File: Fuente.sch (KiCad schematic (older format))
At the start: 14 parts, among them IC1 LM2577HV-ADJ, J1 CONN_01X02, U3 LM7805

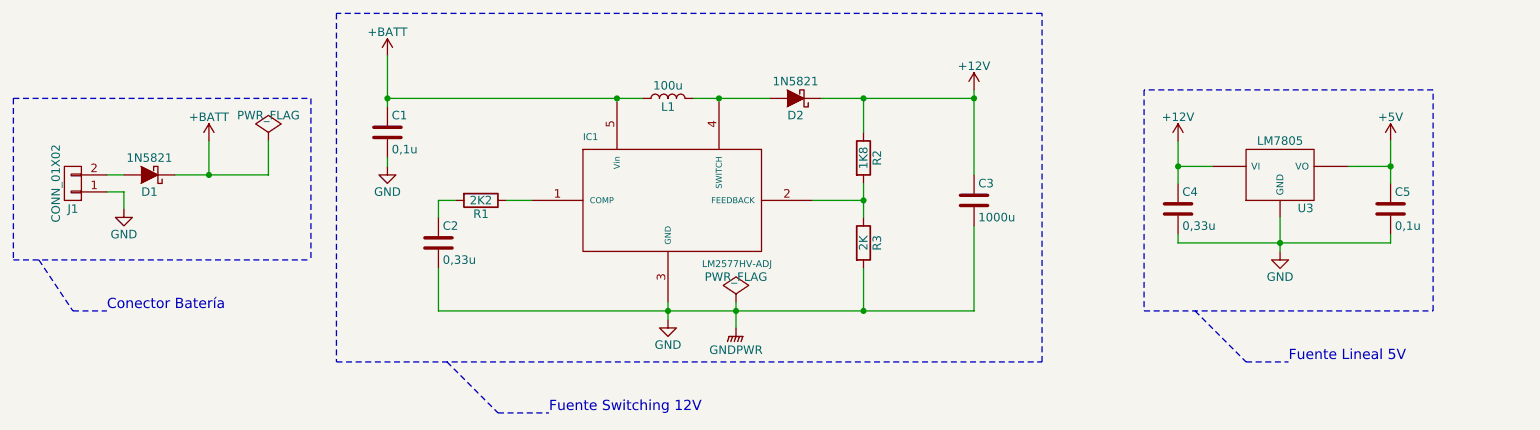
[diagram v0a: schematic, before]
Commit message: Reestructuracion de hojas de esquematico.
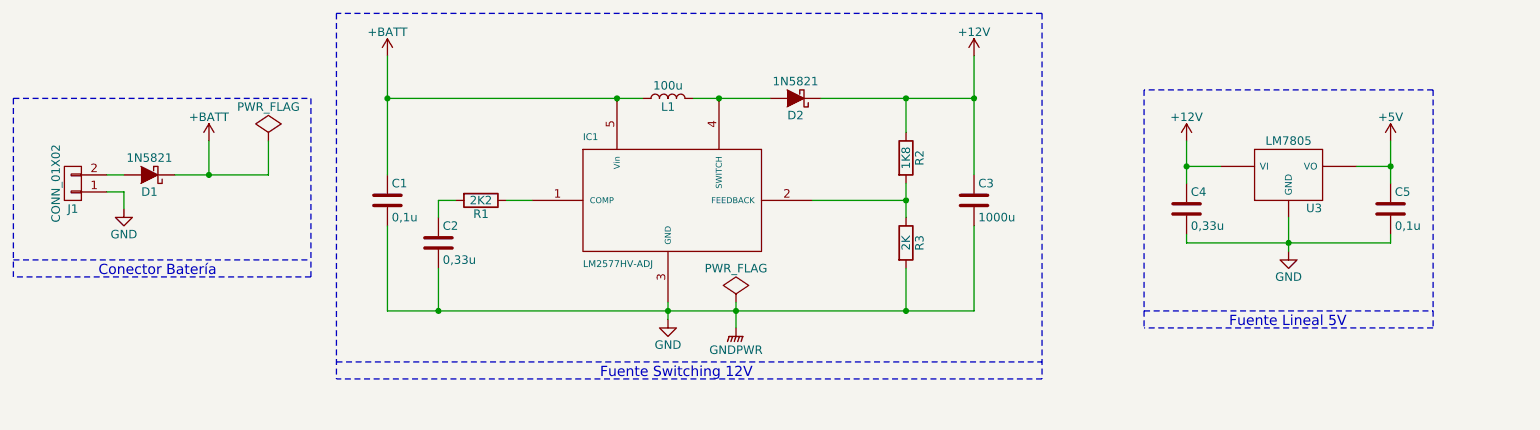
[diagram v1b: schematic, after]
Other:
- moved on the sheet: C1, C4, R2, R3, U3
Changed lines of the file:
@@
 LIBS:contrib
 LIBS:valves
-LIBS:Poncho_Esqueleto
 LIBS:LM2577HV-ADJ
 LIBS:pololu_a4988
@@
 $Descr A4 11693 8268
 encoding utf-8
-Sheet 3 4
+Sheet 3 2
 Title ""
 Date "2017-05-09"
@@
 P 5700 3600
 F 0 "IC1" H 5200 3900 40  0000 L BNN
-F 1 "LM2577HV-ADJ" H 5900 3200 40  0000 L TNN
+F 1 "LM2577HV-ADJ" H 5200 3200 40  0000 L TNN
 F 2 "" H 7300 3450 30  0000 C CIN
 F 3 "" H 7300 3450 60  0000 C CNN
@@
 L R R3
 U 1 1 59114DCA
-P 6850 3900
-F 0 "R3" V 6930 3900 50  0000 C CNN
-F 1 "2K" V 6850 3900 50  0000 C CNN
-F 2 "" V 6780 3900 50  0001 C CNN
-F 3 "" H 6850 3900 50  0001 C CNN
-	1    6850 3900
+P 7100 3900
+F 0 "R3" V 7180 3900 50  0000 C CNN
+F 1 "2K" V 7100 3900 50  0000 C CNN
+F 2 "" V 7030 3900 50  0001 C CNN
+F 3 "" H 7100 3900 50  0001 C CNN
+	1    7100 3900
 	1    0    0    -1
 $EndComp
@@
 L R R2
 U 1 1 59114DE9
-P 6850 3400
-F 0 "R2" V 6930 3400 50  0000 C CNN
-F 1 "1K8" V 6850 3400 50  0000 C CNN
-F 2 "" V 6780 3400 50  0001 C CNN
-F 3 "" H 6850 3400 50  0001 C CNN
-	1    6850 3400
+P 7100 3400
+F 0 "R2" V 7180 3400 50  0000 C CNN
+F 1 "1K8" V 7100 3400 50  0000 C CNN
+F 2 "" V 7030 3400 50  0001 C CNN
+F 3 "" H 7100 3400 50  0001 C CNN
+	1    7100 3400
 	1    0    0    -1
 $EndComp
@@
 L +12V #PWR010
 U 1 1 5911531B
-P 7500 3000
-F 0 "#PWR010" H 7500 2850 50  0001 C CNN
-F 1 "+12V" H 7500 3140 50  0000 C CNN
-F 2 "" H 7500 3000 50  0001 C CNN
-F 3 "" H 7500 3000 50  0001 C CNN
-	1    7500 3000
+P 7500 2800
+F 0 "#PWR010" H 7500 2650 50  0001 C CNN
+F 1 "+12V" H 7500 2940 50  0000 C CNN
+F 2 "" H 7500 2800 50  0001 C CNN
+F 3 "" H 7500 2800 50  0001 C CNN
+	1    7500 2800
 	1    0    0    -1
 $EndComp
@@
 L C C1
 U 1 1 59115966
-P 4050 3250
-F 0 "C1" H 4075 3350 50  0000 L CNN
-F 1 "0,1u" H 4075 3150 50  0000 L CNN
-F 2 "" H 4088 3100 50  0001 C CNN
-F 3 "" H 4050 3250 50  0001 C CNN
-	1    4050 3250
-	1    0    0    -1
-$EndComp
-$Comp
-L GND #PWR011
-U 1 1 591159FB
-P 4050 3450
-F 0 "#PWR011" H 4050 3200 50  0001 C CNN
-F 1 "GND" H 4050 3300 50  0000 C CNN
-F 2 "" H 4050 3450 50  0001 C CNN
-F 3 "" H 4050 3450 50  0001 C CNN
-	1    4050 3450
+P 4050 3650
+F 0 "C1" H 4075 3750 50  0000 L CNN
+F 1 "0,1u" H 4075 3550 50  0000 L CNN
+F 2 "" H 4088 3500 50  0001 C CNN
+F 3 "" H 4050 3650 50  0001 C CNN
+	1    4050 3650
 	1    0    0    -1
 $EndComp
@@
 	5700 4350 5700 4250
 Wire Wire Line
-	6850 3550 6850 3750
-Wire Wire Line
-	6550 3650 6850 3650
-Connection ~ 6850 3650
-Wire Wire Line
-	6850 4050 6850 4300
-Wire Wire Line
-	4350 4300 7500 4300
+	4050 4300 7500 4300
 Connection ~ 5700 4300
 Wire Wire Line
@@
 Wire Wire Line
 	6600 3050 7500 3050
-Wire Wire Line
-	6850 3050 6850 3250
 Connection ~ 6000 3050
 Wire Wire Line
-	7500 3000 7500 3500
-Connection ~ 6850 3050
-Connection ~ 6850 4300
+	7500 2800 7500 3500
 Connection ~ 7500 3050
 Wire Wire Line
@@
 Wire Wire Line
 	4050 3050 5550 3050
-Wire Wire Line
-	4050 2800 4050 3100
 Connection ~ 5400 3050
-Wire Wire Line
-	4050 3400 4050 3450
 $Comp
 L +BATT #PWR012
@@
 	1    0    0    -1
 $EndComp
-Connection ~ 4050 3050
 $Comp
 L CONN_01X02 J1
@@
 L LM7805 U3
 U 1 1 591267BB
-P 9300 3500
-F 0 "U3" H 9450 3304 50  0000 C CNN
-F 1 "LM7805" H 9300 3700 50  0000 C CNN
-F 2 "" H 9300 3500 50  0001 C CNN
-F 3 "" H 9300 3500 50  0001 C CNN
-	1    9300 3500
+P 9350 3500
+F 0 "U3" H 9500 3304 50  0000 C CNN
+F 1 "LM7805" H 9350 3700 50  0000 C CNN
+F 2 "" H 9350 3500 50  0001 C CNN
+F 3 "" H 9350 3500 50  0001 C CNN
+	1    9350 3500
 	1    0    0    -1
 $EndComp
@@
 L GND #PWR015
 U 1 1 5912685A
-P 9300 3950
-F 0 "#PWR015" H 9300 3700 50  0001 C CNN
-F 1 "GND" H 9300 3800 50  0000 C CNN
-F 2 "" H 9300 3950 50  0001 C CNN
-F 3 "" H 9300 3950 50  0001 C CNN
-	1    9300 3950
-	1    0    0    -1
-$EndComp
-Wire Wire Line
-	9300 3950 9300 3750
+P 9350 3950
+F 0 "#PWR015" H 9350 3700 50  0001 C CNN
+F 1 "GND" H 9350 3800 50  0000 C CNN
+F 2 "" H 9350 3950 50  0001 C CNN
+F 3 "" H 9350 3950 50  0001 C CNN
+	1    9350 3950
+	1    0    0    -1
+$EndComp
+Wire Wire Line
+	9350 3950 9350 3750
 $Comp
 L +12V #PWR016
 U 1 1 591269A3
-P 8700 3300
-F 0 "#PWR016" H 8700 3150 50  0001 C CNN
-F 1 "+12V" H 8700 3440 50  0000 C CNN
-F 2 "" H 8700 3300 50  0001 C CNN
-F 3 "" H 8700 3300 50  0001 C CNN
-	1    8700 3300
-	1    0    0    -1
-$EndComp
-Wire Wire Line
-	8700 3300 8700 3550
-Wire Wire Line
-	8700 3450 8900 3450
+P 8750 3300
+F 0 "#PWR016" H 8750 3150 50  0001 C CNN
+F 1 "+12V" H 8750 3440 50  0000 C CNN
+F 2 "" H 8750 3300 50  0001 C CNN
+F 3 "" H 8750 3300 50  0001 C CNN
+	1    8750 3300
+	1    0    0    -1
+$EndComp
+Wire Wire Line
+	8750 3300 8750 3550
+Wire Wire Line
+	8750 3450 8950 3450
 $Comp
 L +5V #PWR017
@@
 	1    0    0    -1
 $EndComp
-Wire Wire Line
-	9950 3300 9950 3550
-Wire Wire Line
-	9950 3450 9700 3450
 $Comp
 L C C4
 U 1 1 59126B8F
-P 8700 3700
-F 0 "C4" H 8725 3800 50  0000 L CNN
-F 1 "0,33u" H 8725 3600 50  0000 L CNN
-F 2 "" H 8738 3550 50  0001 C CNN
-F 3 "" H 8700 3700 50  0001 C CNN
-	1    8700 3700
+P 8750 3700
+F 0 "C4" H 8775 3800 50  0000 L CNN
+F 1 "0,33u" H 8775 3600 50  0000 L CNN
+F 2 "" H 8788 3550 50  0001 C CNN
+F 3 "" H 8750 3700 50  0001 C CNN
+	1    8750 3700
 	1    0    0    -1
 $EndComp
@@
 	1    0    0    -1
 $EndComp
-Wire Wire Line
-	9950 3900 9950 3850
-Wire Wire Line
-	8700 3900 9950 3900
-Connection ~ 9300 3900
-Wire Wire Line
-	8700 3850 8700 3900
-Connection ~ 8700 3450
-Connection ~ 9950 3450
-Wire Notes Line
-	1850 3050 1850 4000
+Connection ~ 9350 3900
+Wire Wire Line
+	8750 3850 8750 3900
+Connection ~ 8750 3450
+Wire Notes Line
+	1850 3050 1850 4100
 Wire Notes Line
 	1850 4000 3600 4000
@@
 	1850 3050 3600 3050
 Wire Notes Line
-	3750 2550 3750 4600
+	3750 2550 3750 4700
 Wire Notes Line
 	3750 4600 7900 4600
 Wire Notes Line
-	7900 4600 7900 2550
+	7900 2550 7900 4700
 Wire Notes Line
 	7900 2550 3750 2550
 Wire Notes Line
-	8500 3000 8500 4300
+	8500 3000 8500 4400
 Wire Notes Line
 	8500 4300 10200 4300
 Wire Notes Line
-	10200 4300 10200 3000
+	10200 3000 10200 4400
 Wire Notes Line
 	10200 3000 8500 3000
-Wire Notes Line
-	2000 4000 2200 4300
-Wire Notes Line
-	2200 4300 2400 4300
-Text Notes 2400 4300 0    60   ~ 0
+Text Notes 2350 4100 0    60   ~ 0
 Conector Batería
-Wire Notes Line
-	4400 4600 4700 4900
-Wire Notes Line
-	4700 4900 5000 4900
-Text Notes 5000 4900 0    60   ~ 0
+Text Notes 5300 4700 0    60   ~ 0
 Fuente Switching 12V
-Wire Notes Line
-	8800 4300 9100 4600
-Wire Notes Line
-	9100 4600 9350 4600
-Text Notes 9350 4600 0    60   ~ 0
+Text Notes 9000 4400 0    60   ~ 0
 Fuente Lineal 5V
 $Comp
@@
 P 3350 3300
 F 0 "#FLG018" H 3350 3375 50  0001 C CNN
-F 1 "PWR_FLAG" H 3350 3450 50  0000 C CNN
+F 1 "PWR_FLAG" H 3350 3500 50  0000 C CNN
 F 2 "" H 3350 3300 50  0001 C CNN
 F 3 "" H 3350 3300 50  0001 C CNN
@@
 Connection ~ 3000 3500
 Wire Notes Line
-	3600 3050 3600 4000
+	3600 3050 3600 4100
 $Comp
 L GNDPWR #PWR019
@@
 P 6100 4250
 F 0 "#FLG?" H 6100 4325 50  0001 C CNN
-F 1 "PWR_FLAG" H 6100 4400 50  0000 C CNN
+F 1 "PWR_FLAG" H 6100 4450 50  0000 C CNN
 F 2 "" H 6100 4250 50  0001 C CNN
 F 3 "" H 6100 4250 50  0001 C CNN
@@
 	1    0    0    -1
 $EndComp
+Wire Notes Line
+	3600 4100 1850 4100
+Wire Notes Line
+	7900 4700 3750 4700
+Wire Notes Line
+	10200 4400 8500 4400
+Wire Wire Line
+	4050 2800 4050 3500
+Connection ~ 4050 3050
+Wire Wire Line
+	4050 3800 4050 4300
+Connection ~ 4350 4300
+Wire Wire Line
+	6550 3650 7100 3650
+Wire Wire Line
+	7100 3550 7100 3750
+Wire Wire Line
+	7100 3250 7100 3050
+Connection ~ 7100 3050
+Connection ~ 7100 3650
+Wire Wire Line
+	7100 4050 7100 4300
+Connection ~ 7100 4300
+Wire Wire Line
+	9750 3450 9950 3450
+Wire Wire Line
+	9950 3300 9950 3550
+Wire Wire Line
+	9950 3900 9950 3850
+Wire Wire Line
+	8750 3900 9950 3900
+Connection ~ 9950 3450
 $EndSCHEMATC

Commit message: Se agregan codigos de DigiKey
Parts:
- C1, C5: Digikey# (none) -> 493-10498-3-ND
- C2, C4: Digikey# (none) -> 493-10258-3-ND
- C3: Digikey# (none) -> 1189-1583-3-ND
- D1, D2: Digikey# (none) -> 1N5821FSCT-ND
- IC1: Digikey# (none) -> LM2577T-ADJ/NOPB-ND
- J1: Digikey# (none) -> 277-1667-ND
- L1: Digikey# (none) -> M8354-ND
- R1: Digikey# (none) -> S2.2KQTR-ND
- R2: Digikey# (none) -> S1.8KQTR-ND
- R3: Digikey# (none) -> S2KQTR-ND
- U3: Digikey# (none) -> LM7805CT-ND
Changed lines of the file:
@@
 $Descr A4 11693 8268
 encoding utf-8
-Sheet 3 2
+Sheet 2 2
 Title ""
 Date "2017-05-09"
@@
 F 2 "" H 7300 3450 30  0000 C CIN
 F 3 "" H 7300 3450 60  0000 C CNN
+F 4 "LM2577T-ADJ/NOPB-ND" H 5700 3600 60  0001 C CNN "Digikey#"
 	1    5700 3600
 	1    0    0    -1
@@
 F 2 "" V 7030 3900 50  0001 C CNN
 F 3 "" H 7100 3900 50  0001 C CNN
+F 4 "S2KQTR-ND" H 7100 3900 60  0001 C CNN "Digikey#"
 	1    7100 3900
 	1    0    0    -1
@@
 F 2 "" V 7030 3400 50  0001 C CNN
 F 3 "" H 7100 3400 50  0001 C CNN
+F 4 "S1.8KQTR-ND" H 7100 3400 60  0001 C CNN "Digikey#"
 	1    7100 3400
 	1    0    0    -1
@@
 F 2 "" H 5700 3050 50  0001 C CNN
 F 3 "" H 5700 3050 50  0001 C CNN
+F 4 "M8354-ND" H 5700 3050 60  0001 C CNN "Digikey#"
 	1    5700 3050
 	0    -1   -1   0
@@
 F 2 "" H 6450 3050 50  0001 C CNN
 F 3 "" H 6450 3050 50  0001 C CNN
+F 4 "1N5821FSCT-ND" H 6450 3050 60  0001 C CNN "Digikey#"
 	1    6450 3050
 	-1   0    0    1
@@
 F 2 "" H 7538 3500 50  0001 C CNN
 F 3 "" H 7500 3650 50  0001 C CNN
+F 4 "1189-1583-3-ND" H 7500 3650 60  0001 C CNN "Digikey#"
 	1    7500 3650
 	1    0    0    -1
@@
 F 2 "" V 4530 3650 50  0001 C CNN
 F 3 "" H 4600 3650 50  0001 C CNN
+F 4 "S2.2KQTR-ND" H 4600 3650 60  0001 C CNN "Digikey#"
 	1    4600 3650
 	0    1    1    0
@@
 F 2 "" H 4388 3750 50  0001 C CNN
 F 3 "" H 4350 3900 50  0001 C CNN
+F 4 "493-10258-3-ND" H 4350 3900 60  0001 C CNN "Digikey#"
 	1    4350 3900
 	1    0    0    -1
@@
 F 2 "" H 4088 3500 50  0001 C CNN
 F 3 "" H 4050 3650 50  0001 C CNN
+F 4 "493-10498-3-ND" H 4050 3650 60  0001 C CNN "Digikey#"
 	1    4050 3650
 	1    0    0    -1
@@
 F 2 "" H 2200 3550 50  0001 C CNN
 F 3 "" H 2200 3550 50  0001 C CNN
+F 4 "277-1667-ND" H 2200 3550 60  0001 C CNN "Digikey#"
 	1    2200 3550
 	-1   0    0    1
@@
 F 2 "" H 2650 3500 50  0001 C CNN
 F 3 "" H 2650 3500 50  0001 C CNN
+F 4 "1N5821FSCT-ND" H 2650 3500 60  0001 C CNN "Digikey#"
 	1    2650 3500
 	-1   0    0    1
@@
 F 2 "" H 9350 3500 50  0001 C CNN
 F 3 "" H 9350 3500 50  0001 C CNN
+F 4 "LM7805CT-ND" H 9350 3500 60  0001 C CNN "Digikey#"
 	1    9350 3500
 	1    0    0    -1
@@
 F 2 "" H 8788 3550 50  0001 C CNN
 F 3 "" H 8750 3700 50  0001 C CNN
+F 4 "493-10258-3-ND" H 8750 3700 60  0001 C CNN "Digikey#"
 	1    8750 3700
 	1    0    0    -1
@@
 F 2 "" H 9988 3550 50  0001 C CNN
 F 3 "" H 9950 3700 50  0001 C CNN
+F 4 "493-10498-3-ND" H 9950 3700 60  0001 C CNN "Digikey#"
 	1    9950 3700
 	1    0    0    -1

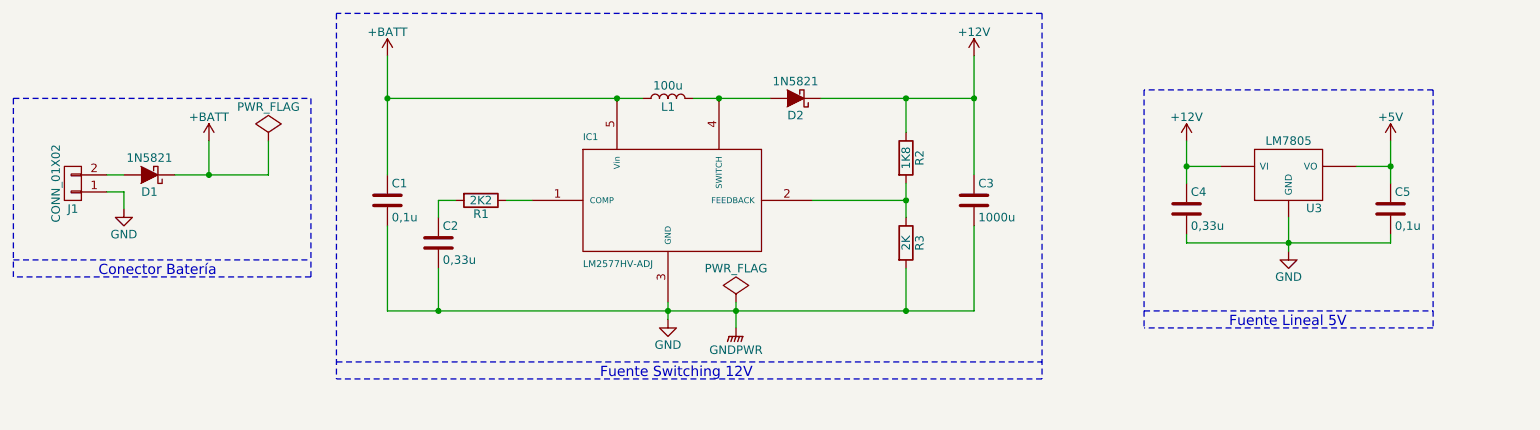
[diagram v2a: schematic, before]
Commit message: Se aplican las primeras correciones del profesor sobre esquematico
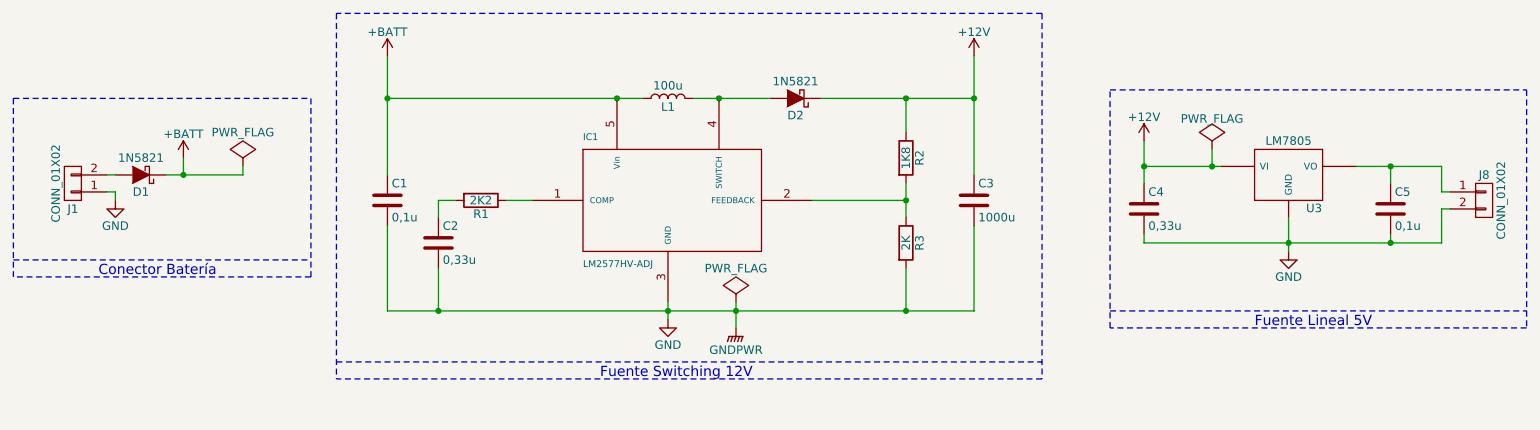
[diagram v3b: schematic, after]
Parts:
- added J8: CONN_01X02, symbol CONN_01X02
- C1, C5: Manf (none) -> Nichicon; Manf# (none) -> UKL1H0R1MDD1TD
- C2, C4: Manf (none) -> Nichicon; Manf# (none) -> UMP1HR33MDD1TP
- C3: Manf (none) -> Rubycon; Manf# (none) -> 25PX1000MEFCT810X16
- D1, D2: Manf (none) -> Fairchild/ON Semiconductor; Manf# (none) -> 1N5821
- IC1: Manf (none) -> Texas Instruments; Manf# (none) -> LM2577T-ADJ/NOPB
- J1: Manf (none) -> Phoenix Contact; Manf# (none) -> 1935161
- L1: Manf (none) -> Bourns Inc.; Manf# (none) -> 1120-101K-RC
- R1: Manf (none) -> Stackpole Electronics Inc.; Manf# (none) -> CFM14JT2K20
- R2: Manf (none) -> Stackpole Electronics Inc.; Manf# (none) -> CFM14JT1K80
- R3: Manf (none) -> Stackpole Electronics Inc.; Manf# (none) -> CFM14JT2K00
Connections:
- net GND: now also J8.2 (P2)
- net +5V: no longer names the net of C5.1, U3.VO
- net +5V: now also J8.1 (P1)
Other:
- moved on the sheet: C4, D1
